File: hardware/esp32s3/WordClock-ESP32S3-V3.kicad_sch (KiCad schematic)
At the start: 97 parts, among them Q1 SI7149DP-T1-GE3, Q2 MMBF170, Q3 SI7149DP-T1-GE3, SW1 K2-1157SP-I4SW-01, SW2 K2-1157SP-I4SW-01, SW3 K2-1157SP-I4SW-01, SW5 K2-1157SP-I4SW-01, U1 DS18B20, U10 SY8301ABC, U11 USBLC6-2SC6, U2 ESP32-S3-WROOM-1-N8, U3 SN74AHCT1G125DBVR, U5 DS3231MZ+TRL, U6 AT24C32M/TR, U7 SMTU2032-LF, U9 TPS2121RUXR

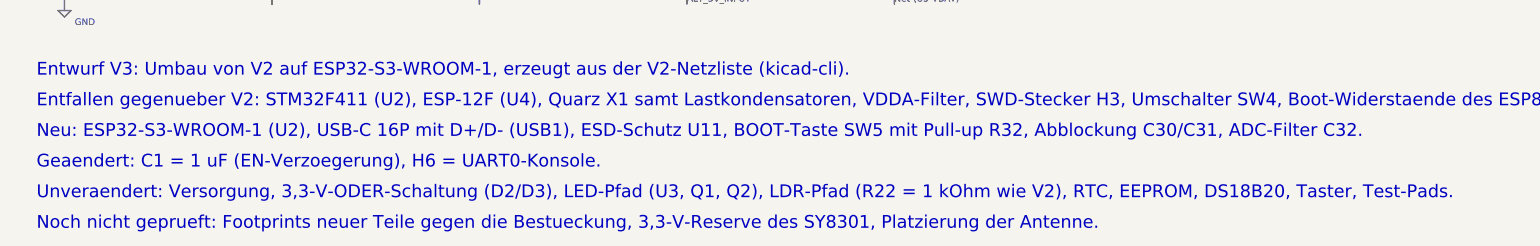
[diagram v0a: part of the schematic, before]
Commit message: Hardware: Stückliste des V3-Entwurfs mit geprüften LCSC-Nummern, drei falsche Felder korrigiert
bom.py erzeugt aus dem Schaltplan bom.csv (V2-Format) und bom-arbeit.csv mit Klasse und Prüfdatum: 47 Zeilen,
83 Bauteile, 17 Basic, 30 Extended, keine Zeile offen. H4 prüft jetzt, statt zu warnen. Korrigiert: R23
trug die Nummer von R19 (jetzt C17520), C30 (10 µF) die 100-nF-Nummer (jetzt C15850), C1 (1 µF) ebenso
(jetzt C28323). Die neuen Teile U2, USB1 und U11 bekommen das Feld LCSC. jlcpcb-bestand.md: R22 bleibt
1 kΩ, R23 und C10 als Zeilen ergänzt (44 Zeilen, 75 Bauteile).

Co-Authored-By: Claude Sonnet 5.5 <noreply@anthropic.com>
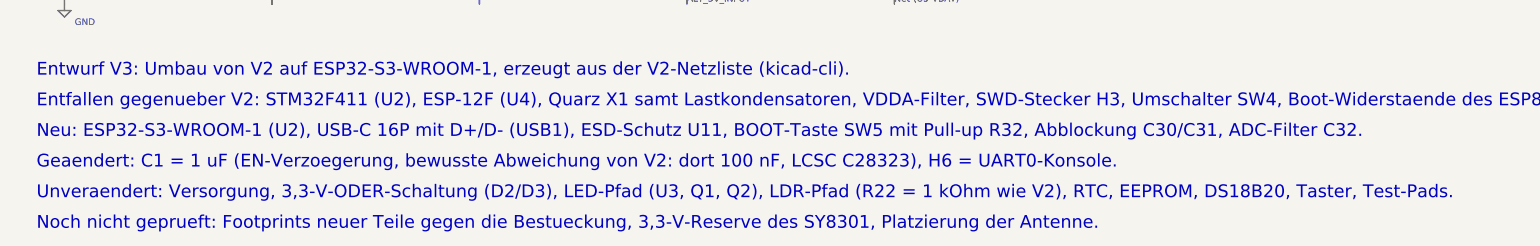
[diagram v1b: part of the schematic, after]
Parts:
- C1: LCSC C49678 -> C28323
- C30: LCSC C49678 -> C15850
- R23: LCSC C17841 -> C17520
- U11: LCSC (none) -> C7519
- U2: LCSC (none) -> C2913198
- USB1: LCSC (none) -> C165948
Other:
- note added: "Geaendert: C1 = 1 uF (EN-Verzoegerung, bewusste Abweichung von V2: dort 100 nF, LCSC C28323), H6 = UART0-Konsole."
- note removed: "Geaendert: C1 = 1 uF (EN-Verzoegerung), H6 = UART0-Konsole."

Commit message: Hardware: Konsole H6 nach V2-Belegung, USB-Reihenwiderstände, C30 22 µF, R29 31,6 kΩ, C32 unbestückt
Pinregeln für TXD0/RXD0/USB nachgezogen; H1-H8 und 21 Gegenproben grün.

Co-Authored-By: Claude Sonnet 5.5 <noreply@anthropic.com>
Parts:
- added C33: 100nF, Capacitor_SMD:C_0805_2012Metric, symbol Device:C
- added C34, C35: DNP (Wert offen), Capacitor_SMD:C_0805_2012Metric, symbol Device:C
- added R33: 510Ω, Capacitor_SMD:C_0805_2012Metric, symbol Device:R
- added R34, R35: 0Ω, Resistor_SMD:R_0805_2012Metric, symbol Device:R
- added R36: DNP (Wert+Schiene ungeprueft), Resistor_SMD:R_0805_2012Metric, symbol Device:R
- C30: value 10uF -> 22uF; LCSC C15850 -> C45783
- C32: now not fitted
- R29: value 32kΩ -> 31.6kΩ
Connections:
- net GND: now also C33.2, C34.2, C35.2
- net RX_UART: now also R33.2; no longer U2.36 (RXD0)
- net TX_UART: now also U2.36 (RXD0); no longer U2.37 (TXD0)
- net USB_5V_INPUT: now also C33.1
- net USB_DN: now also R35.1; no longer U2.13 (USB_D-)
- net USB_DP: now also R34.1; no longer U2.14 (USB_D+)
- net VCC_3.3V: now also R36.2
- new net UART0_TXD: R33.1, U2.37 (TXD0)
- new net USB_DN_M: C35.1, R35.2, U2.13 (USB_D-)
- new net USB_DP_M: C34.1, R34.2, R36.1, U2.14 (USB_D+)
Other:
- note added: "Geaendert: C1 = 1 uF (EN-Verzoegerung, bewusste Abweichung von V2: dort 100 nF, LCSC C28323), H6 = UART0-Konsole (TXD0 -> R33 -> RX_UART/H6.3, RXD0 <- TX_UART/H6.2, wie V2-Belegung), R29 = 31,6 kOhm (Wert des Teils C2930156)."
- note added: "Neu: ESP32-S3-WROOM-1 (U2), USB-C 16P (USB1), ESD-Schutz U11 mit C33 am VBUS-Pin, 0-Ohm-Bruecken R34/R35 in D+/D- (Modulseite USB_DP_M/USB_DN_M), BOOT-Taste SW5 mit Pull-up R32, Abblockung C30 (22 uF)/C31, R33 (510 Ohm) in TXD0."
- note added: "Unbestueckte Plaetze (DNP, AE-02): C34/C35 (USB-Leitungen nach GND), R36 (D+-Pull-up; Wert und Schiene UNGEPRUEFT, 3,3 V nur als Platzhalter). C32 (ADC-Filter, Antrag A1): UNBESTUECKT (dnp), Freigabe des Nutzers fehlt; Platz bleibt."
- note removed: "Geaendert: C1 = 1 uF (EN-Verzoegerung, bewusste Abweichung von V2: dort 100 nF, LCSC C28323), H6 = UART0-Konsole."
- note removed: "Neu: ESP32-S3-WROOM-1 (U2), USB-C 16P mit D+/D- (USB1), ESD-Schutz U11, BOOT-Taste SW5 mit Pull-up R32, Abblockung C30/C31, ADC-Filter C32."

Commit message: Hardware: Schaltplan V3 in V2-Blockanordnung auf einem Blatt (A2), Netzliste unverändert
Co-Authored-By: Claude Sonnet 5.5 <noreply@anthropic.com>
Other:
- note added: "(ADC-Filter, Antrag A1): UNBESTUECKT (dnp), Freigabe des Nutzers fehlt;"
- note added: "(D+-Pull-up; Wert und Schiene UNGEPRUEFT, 3,3 V nur als Platzhalter). C32"
- note added: "(kicad-cli). Anordnung der Bloecke wie in V2 (ein Blatt, Funktionsbloecke"
- note added: "1 > VCC_3.3V"
- note added: "2 > TX"
- note added: "3 > RX"
- note added: "4 > GND"
- note added: "BOOT1: R10 (kein BOOT1-Pin)"
- note added: "DCF77 Ersatz"
- note added: "DS18B20"
- note added: "DS3231"
- note added: "ESP12F: U4, R14, R15, R16, R18 (Boot-Beschaltung ESP8266)"
- note added: "ESP32-S3-WROOM-1 (U2) mit Strapping/BOOT/EN"
- note added: "Entfaellt gegenueber V2"
- note added: "Entfallen gegenueber V2: STM32F411 (U2), ESP-12F (U4), Quarz X1 samt"
- note added: "Entwurf V3: Umbau von V2 auf ESP32-S3-WROOM-1, erzeugt aus der V2-Netzliste"
- note added: "Geaendert: C1 = 1 uF (EN-Verzoegerung, bewusste Abweichung von V2: dort 100 nF,"
- note added: "Hinweise zum Entwurf V3"
- note added: "LCSC C28323), H6 = UART0-Konsole (TXD0 -> R33 -> RX_UART/H6.3, RXD0 <-"
- note added: "LDR-Pfad (R22 = 1 kOhm wie V2), RTC, EEPROM, DS18B20, Taster, Test-Pads."
- note added: "LED Controll"
- note added: "LED Power"
- note added: "LED-Board-Connector"
- note added: "Lastkondensatoren, VDDA-Filter, SWD-Stecker H3, Umschalter SW4, Boot-"
- note added: "Led STM"
- note added: "Neu: ESP32-S3-WROOM-1 (U2), USB-C 16P (USB1), ESD-Schutz U11 mit C33 am VBUS-"
- note added: "Noch nicht geprueft: Footprints neuer Teile gegen die Bestueckung, 3,3-V-Reserve"
- note added: "Oscillator: X1, C3, C5, R7 (der S3 braucht keinen Quarz)"
- note added: "PWR_FLAG (Markierung fuer die Pruefung der Versorgung)"
- note added: "Pin, 0-Ohm-Bruecken R34/R35 in D+/D- (Modulseite USB_DP_M/USB_DN_M), BOOT-"
- note added: "Platz bleibt."
- note added: "PowerSupply"
- note added: "Reset"
- note added: "Reset: R2 (Pull-up) und Schalter SW4 (RUN/PROG) in UART"
- note added: "STM32 Prog.: H3 (SWD), D1 (Programmierung ueber USB/UART0)"
- note added: "STM32: U2 STM32F411, C9, C11, C14, L1 (VDDA-Filter)"
- note added: "Switches"
- note added: "TSOP Ersatz"
- note added: "TXD0."
- note added: "TX_UART/H6.2, wie V2-Belegung), R29 = 31,6 kOhm (Wert des Teils C2930156)."
- note added: "Taste SW5 mit Pull-up R32, Abblockung C30 (22 uF)/C31, R33 (510 Ohm) in"
- note added: "UART"
- note added: "USB-C"
- note added: "Unbestueckte Plaetze (DNP, AE-02): C34/C35 (USB-Leitungen nach GND), R36"
- note added: "Unveraendert: Versorgung, 3,3-V-ODER-Schaltung (D2/D3), LED-Pfad (U3, Q1, Q2),"
- note added: "Widerstaende des ESP8266."
- note added: "des SY8301, Platzierung der Antenne."
- note added: "mit Titel)."
- note removed: "ESP32-S3-WROOM-1 mit Reset, Boot und Konsole"
- note removed: "Entfallen gegenueber V2: STM32F411 (U2), ESP-12F (U4), Quarz X1 samt Lastkondensatoren, VDDA-Filter, SWD-Stecker H3, Umschalter SW4, Boot-Widerstaende des ESP8266."
- note removed: "Entwurf V3: Umbau von V2 auf ESP32-S3-WROOM-1, erzeugt aus der V2-Netzliste (kicad-cli)."
- note removed: "Geaendert: C1 = 1 uF (EN-Verzoegerung, bewusste Abweichung von V2: dort 100 nF, LCSC C28323), H6 = UART0-Konsole (TXD0 -> R33 -> RX_UART/H6.3, RXD0 <- TX_UART/H6.2, wie V2-Belegung), R29 = 31,6 kOhm (Wert des Teils C2930156)."
- note removed: "LED-Ausgang, Pegelwandler und 5-V-Schalter"
- note removed: "Neu: ESP32-S3-WROOM-1 (U2), USB-C 16P (USB1), ESD-Schutz U11 mit C33 am VBUS-Pin, 0-Ohm-Bruecken R34/R35 in D+/D- (Modulseite USB_DP_M/USB_DN_M), BOOT-Taste SW5 mit Pull-up R32, Abblockung C30 (22 uF)/C31, R33 (510 Ohm) in TXD0."
- note removed: "Noch nicht geprueft: Footprints neuer Teile gegen die Bestueckung, 3,3-V-Reserve des SY8301, Platzierung der Antenne."
- note removed: "Sensoren, RTC und EEPROM"
- note removed: "USB-C, Eingangsschutz und Power-Mux"
- note removed: "Unbestueckte Plaetze (DNP, AE-02): C34/C35 (USB-Leitungen nach GND), R36 (D+-Pull-up; Wert und Schiene UNGEPRUEFT, 3,3 V nur als Platzhalter). C32 (ADC-Filter, Antrag A1): UNBESTUECKT (dnp), Freigabe des Nutzers fehlt; Platz bleibt."
- note removed: "Unveraendert: Versorgung, 3,3-V-ODER-Schaltung (D2/D3), LED-Pfad (U3, Q1, Q2), LDR-Pfad (R22 = 1 kOhm wie V2), RTC, EEPROM, DS18B20, Taster, Test-Pads."
- note removed: "Versorgung 5 V und 3,3 V"

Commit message: Hardware: V3-Schaltplan als V2-Blatt (A3) mit gezeichneten Drähten, geänderte Blöcke neu; H1-H9 und 23 Gegenproben grün
Unveränderte V2-Blöcke aus der V2-Datei übernommen (88 Bauteile, 0 Nachbarabweichungen),
Stummelanteil 0,23, 0 sichtbare Net-(. Footprints R27/R30/R33, R17-LCSC, DNP-Felder berichtigt.

Co-Authored-By: Claude Sonnet 5.5 <noreply@anthropic.com>
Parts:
- C32: now left out of the parts list
- C34, C35: LCSC C49678 -> (none); now left out of the parts list
- R17: LCSC (none) -> C17477
- R27, R30, R33: footprint Capacitor_SMD:C_0805_2012Metric -> Resistor_SMD:R_0805_2012Metric
- R36: LCSC C17414 -> (none); now left out of the parts list
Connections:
- net Net-(C10-Pad2): no longer names the net of C10.2, Q1.4, R23.2
- net Net-(C2-Pad2): no longer names the net of C2.2, R24.2, R25.1
- net Net-(D2-A): no longer names the net of C27.1, C28.1, C29.1, D2.2 (A), L2.2
- net Net-(D3-A): no longer names the net of D3.2 (A), H6.1
- net Net-(F2-Pad2): no longer names the net of F2.2, Q3.5, Q3.6, Q3.7, Q3.8, Q3.9, TP5.1
- net Net-(LED1-A): no longer names the net of LED1.2 (A), R6.2
- net Net-(LED4-A): no longer names the net of LED4.2 (A), R27.2
- net Net-(LED5-A): no longer names the net of LED5.2 (A), R30.2
- net Net-(Q2-D): no longer names the net of Q2.3 (D), R21.2, R23.1
- net Net-(Q2-G): no longer names the net of Q2.1 (G), R19.2, R20.1
- net Net-(Q3-Pad4): no longer names the net of Q3.4, R24.1
- net Net-(R1-Pad2): no longer names the net of R1.2, SW2.1
- net Net-(U10-BS): no longer names the net of C25.1, U10.1 (BS)
- net Net-(U10-FB): no longer names the net of R28.1, R29.1, U10.3 (FB)
- net Net-(U10-LX): no longer names the net of C25.2, L2.1, U10.6 (LX)
- net Net-(U3-VCC): no longer names the net of R13.1, R17.1, U3.5 (VCC)
- net Net-(U3-Y): no longer names the net of R11.1, U3.4 (Y)
- net Net-(U5-VBAT): no longer names the net of U5.6 (VBAT), U7.1
- net Net-(U6-E0): no longer names the net of RN1.7, U6.1 (E0)
- net Net-(U6-E1): no longer names the net of RN1.6, U6.2 (E1)
- net Net-(U6-E2): no longer names the net of RN1.5, U6.3 (E2)
- net Net-(U9-ILM): no longer names the net of R26.2, U9.10 (ILM)
- net Net-(U9-SS): no longer names the net of C24.2, U9.11 (SS)
- net Net-(USB1-CC1) renamed USB_CC1
- net Net-(USB1-CC2) renamed USB_CC2
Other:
- note added: "(R12)."
- note added: "1 > VCC_3.3V 2 > TX 3 > RX 4 > GND"
- note added: "Alte USB-Buchse 6P (USB1)"
- note added: "C11, C14, L1 (VDDA-Filter)"
- note added: "C34, C35, R36 unbestueckt (DNP), Wert offen;"
- note added: "DNP: C32, C34, C35, R36. Ungeprueft:"
- note added: "EN: R12, C1, SW3 (Block Reset)"
- note added: "ESP-12F (U4), R14-R16, R18"
- note added: "ESP32-S3, USB-C, BOOT, UART (R33), Reset"
- note added: "ESP32-S3-WROOM-1 (U2)"
- note added: "Footprints, SY8301-Reserve, Antenne."
- note added: "IO0 = BOOT (Strapping)"
- note added: "IO3/IO45/IO46 offen"
- note added: "Neu: U2, USB1, U11, C30, C31, C33, R32-R35,"
- note added: "Oszillator X1, C3, C5, R7"
- note added: "R34/R35: 0-Ohm-Bruecken in D+/D-."
- note added: "R36: Schiene UNGEPRUEFT."
- note added: "Reset: R2; Umschalter SW4"
- note added: "STM32F411 (U2 alt), C9,"
- note added: "SW5. Geaendert: C1 1 uF, R29 31,6k."
- note added: "SWD H3, D1; BOOT1 R10"
- note added: "U11: Pin 1/6 = USB_DP, Pin 3/4 = USB_DN,"
- note added: "V3 aus V2: Bloecke 1:1 uebernommen, neu:"
- note added: "ueber gleichnamige Beschriftung verbunden."
- note removed: "(ADC-Filter, Antrag A1): UNBESTUECKT (dnp), Freigabe des Nutzers fehlt;"
- note removed: "(D+-Pull-up; Wert und Schiene UNGEPRUEFT, 3,3 V nur als Platzhalter). C32"
- note removed: "(kicad-cli). Anordnung der Bloecke wie in V2 (ein Blatt, Funktionsbloecke"
- note removed: "1 > VCC_3.3V"
- note removed: "2 > TX"
- note removed: "3 > RX"
- note removed: "4 > GND"
- note removed: "BOOT1: R10 (kein BOOT1-Pin)"
- note removed: "Befestigung"
- note removed: "ESP12F: U4, R14, R15, R16, R18 (Boot-Beschaltung ESP8266)"
- note removed: "ESP32-S3-WROOM-1 (U2) mit Strapping/BOOT/EN"
- note removed: "Entfallen gegenueber V2: STM32F411 (U2), ESP-12F (U4), Quarz X1 samt"
- note removed: "Entwurf V3: Umbau von V2 auf ESP32-S3-WROOM-1, erzeugt aus der V2-Netzliste"
- note removed: "Geaendert: C1 = 1 uF (EN-Verzoegerung, bewusste Abweichung von V2: dort 100 nF,"
- note removed: "LCSC C28323), H6 = UART0-Konsole (TXD0 -> R33 -> RX_UART/H6.3, RXD0 <-"
- note removed: "LDR-Pfad (R22 = 1 kOhm wie V2), RTC, EEPROM, DS18B20, Taster, Test-Pads."
- note removed: "Lastkondensatoren, VDDA-Filter, SWD-Stecker H3, Umschalter SW4, Boot-"
- note removed: "Neu: ESP32-S3-WROOM-1 (U2), USB-C 16P (USB1), ESD-Schutz U11 mit C33 am VBUS-"
- note removed: "Noch nicht geprueft: Footprints neuer Teile gegen die Bestueckung, 3,3-V-Reserve"
- note removed: "Oscillator: X1, C3, C5, R7 (der S3 braucht keinen Quarz)"
- note removed: "PWR_FLAG (Markierung fuer die Pruefung der Versorgung)"
- note removed: "Pin, 0-Ohm-Bruecken R34/R35 in D+/D- (Modulseite USB_DP_M/USB_DN_M), BOOT-"
- note removed: "Platz bleibt."
- note removed: "Reset: R2 (Pull-up) und Schalter SW4 (RUN/PROG) in UART"
- note removed: "STM32 Prog.: H3 (SWD), D1 (Programmierung ueber USB/UART0)"
- note removed: "STM32: U2 STM32F411, C9, C11, C14, L1 (VDDA-Filter)"
- note removed: "TXD0."
- note removed: "TX_UART/H6.2, wie V2-Belegung), R29 = 31,6 kOhm (Wert des Teils C2930156)."
- note removed: "Taste SW5 mit Pull-up R32, Abblockung C30 (22 uF)/C31, R33 (510 Ohm) in"
- note removed: "Unbestueckte Plaetze (DNP, AE-02): C34/C35 (USB-Leitungen nach GND), R36"
- note removed: "Unveraendert: Versorgung, 3,3-V-ODER-Schaltung (D2/D3), LED-Pfad (U3, Q1, Q2),"
- note removed: "Widerstaende des ESP8266."
- note removed: "des SY8301, Platzierung der Antenne."
- note removed: "mit Titel)."
